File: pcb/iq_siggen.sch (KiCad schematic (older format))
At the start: 109 parts, among them J1 J3 - BANK0, J10 Barrel_Jack_MountingPin, J11 Conn_Coaxial, J12 Conn_01x01_Male, J13 Conn_01x01_Male, J14 Conn_01x01_Male, J15 Conn_01x01_Male, J16 Conn_01x01_Male, J17 Conn_01x01_Male, J2 J4 - BANK1, J3 Conn_01x20_Male, J4 Conn_01x01_Male, J6 Conn_Coaxial, J7 Conn_Coaxial, J8 Conn_Coaxial, J9 Conn_Coaxial, SW1 SW_Push, SW2 SW_Push, SW3 SW_Push, SW4 SW_Push, U1 AMS1117-3.3, U2 TPS72325DBVR, U3 TLV73325PDBVT

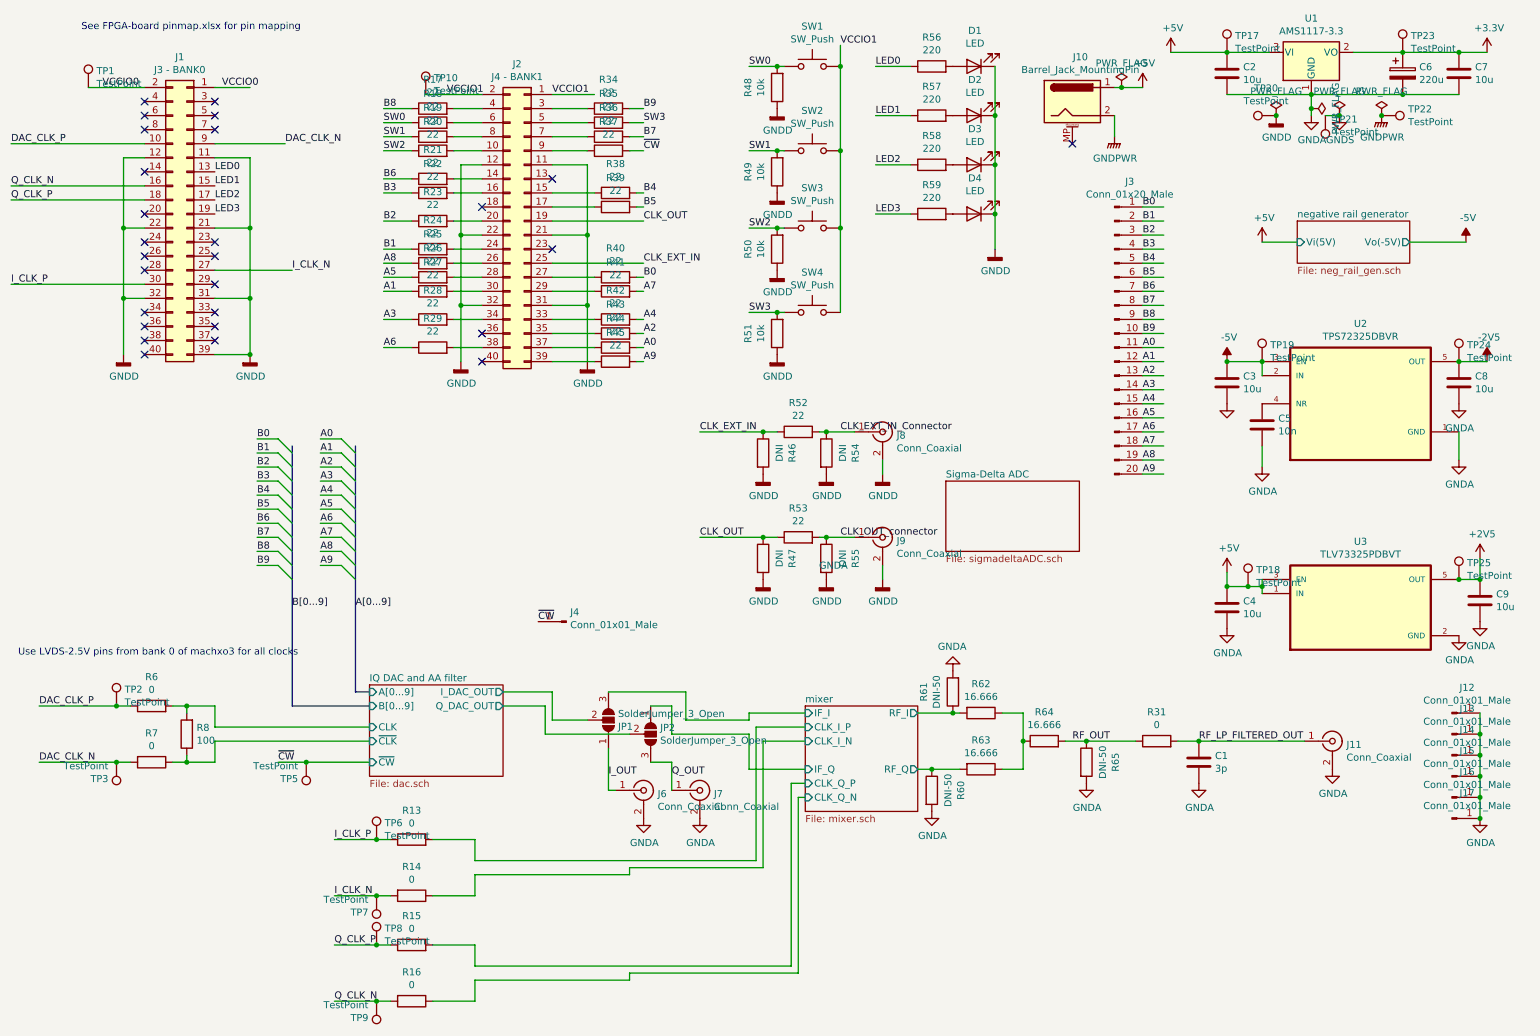
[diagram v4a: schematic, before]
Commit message: routing contiued, add swtiches, remove test points, all parts now positioned on board
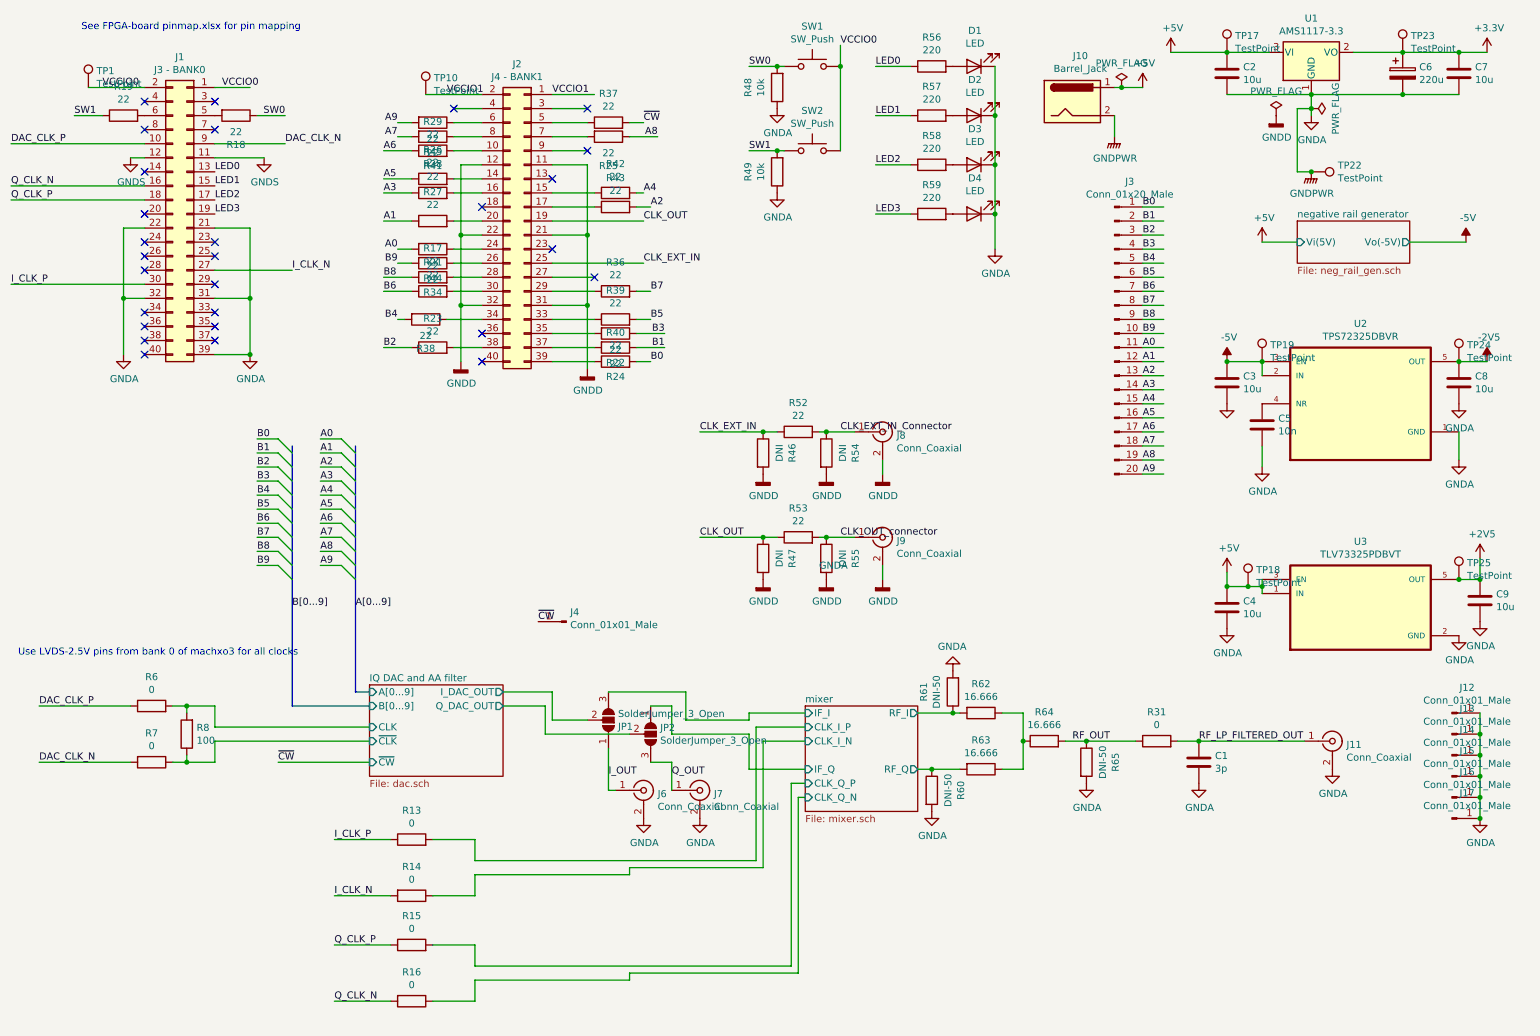
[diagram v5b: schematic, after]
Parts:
- removed J10: Barrel_Jack_MountingPin, Connector_BarrelJack:BarrelJack_Horizontal, symbol Connector:Barrel_Jack_MountingPin
- removed R20, R35: 22, Resistor_SMD:R_0603_1608Metric, symbol Device:R
- removed R50, R51: 10k, Resistor_SMD:R_0603_1608Metric, symbol Device:R
- removed SW3, SW4: SW_Push, symbol Switch:SW_Push
- removed TP2, TP20, TP21, TP3, TP5, TP6, TP7, TP8, TP9: TestPoint, TestPoint:TestPoint_Pad_D1.5mm, symbol Connector:TestPoint
- added J10: Barrel_Jack, Connector_BarrelJack:BarrelJack_Horizontal, symbol Connector:Barrel_Jack
- SW1, SW2: footprint (none) -> Button_Switch_THT:SW_PUSH_6mm_H5mm
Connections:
- net labels removed: SW2, SW3
- wire segments 270 -> 255
- no-connect marks 27 -> 28
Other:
- moved on the sheet: R17, R18, R19, R21, R22, R23, R24, R25, R26, R27, R28, R29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

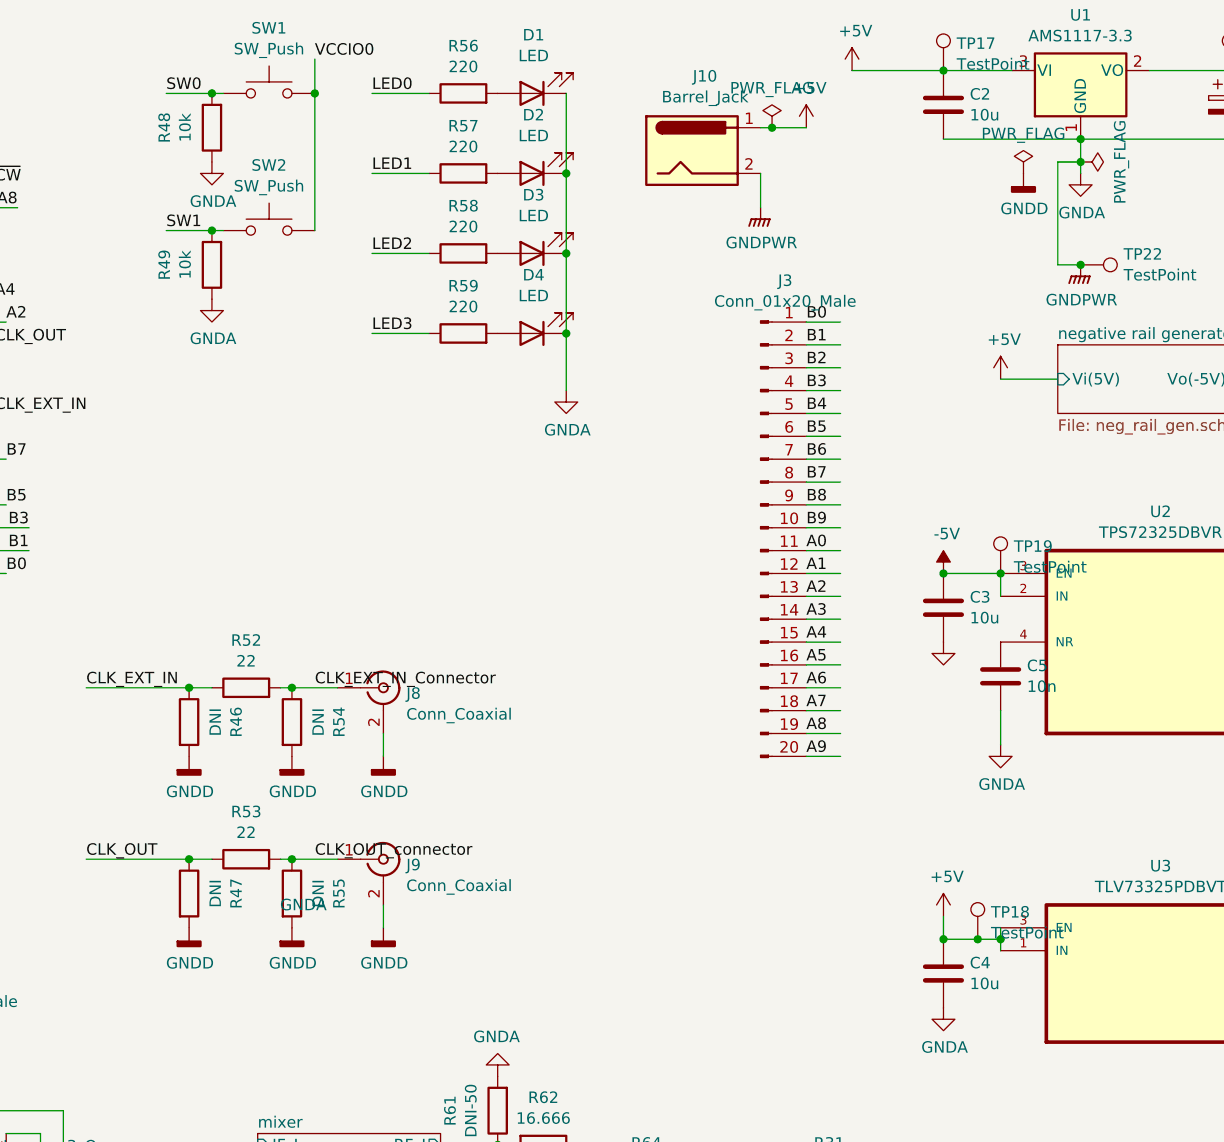
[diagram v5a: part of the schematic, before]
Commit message: layout refininements, stitching vias
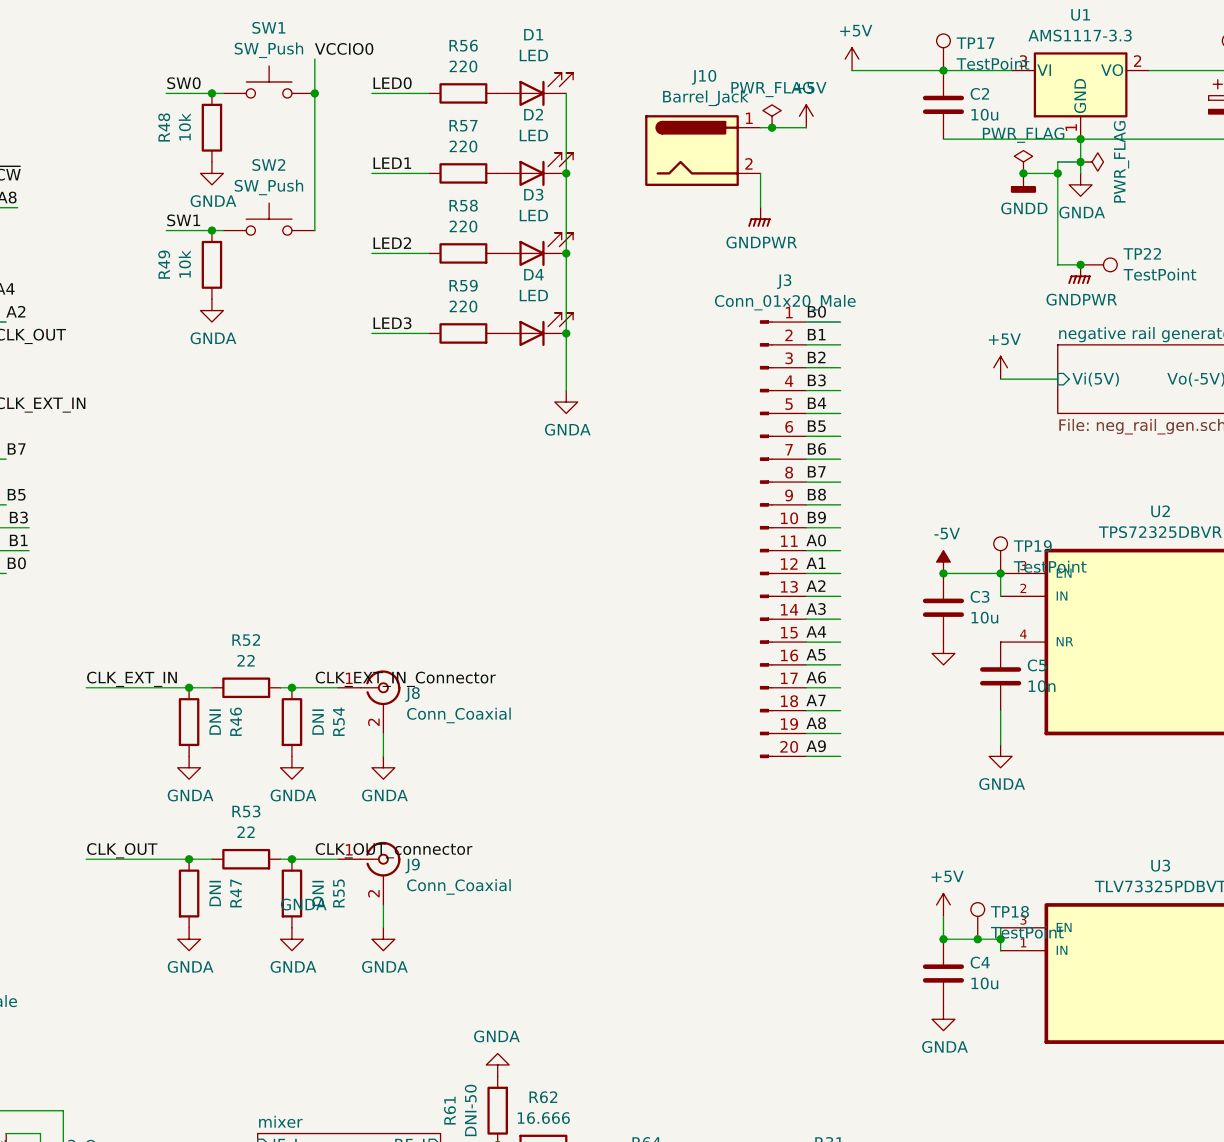
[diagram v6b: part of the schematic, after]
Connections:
- wire segments 255 -> 257
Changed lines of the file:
@@
 Text Label 5400 3550 0    50   ~ 0
 CLK_EXT_IN
-$Comp
-L power:GNDD #PWR017
-U 1 1 608214B8
-P 6700 3850
-AR Path="/608214B8" Ref="#PWR017"  Part="1"
-AR Path="/5FB3742F/608214B8" Ref="#PWR?"  Part="1"
-F 0 "#PWR017" H 6700 3600 50  0001 C CNN
-F 1 "GNDD" H 6704 3695 50  0000 C CNN
-F 2 "" H 6700 3850 50  0001 C CNN
-F 3 "" H 6700 3850 50  0001 C CNN
-	1    6700 3850
-	1    0    0    -1
-$EndComp
 Wire Wire Line
 	6500 3550 6300 3550
@@
 Wire Wire Line
 	5850 3550 5400 3550
-$Comp
-L power:GNDD #PWR015
-U 1 1 60891A86
-P 6300 3850
-AR Path="/60891A86" Ref="#PWR015"  Part="1"
-AR Path="/5FB3742F/60891A86" Ref="#PWR?"  Part="1"
-F 0 "#PWR015" H 6300 3600 50  0001 C CNN
-F 1 "GNDD" H 6304 3695 50  0000 C CNN
-F 2 "" H 6300 3850 50  0001 C CNN
-F 3 "" H 6300 3850 50  0001 C CNN
-	1    6300 3850
-	1    0    0    -1
-$EndComp
-$Comp
-L power:GNDD #PWR09
-U 1 1 60891D84
-P 5850 3850
-AR Path="/60891D84" Ref="#PWR09"  Part="1"
-AR Path="/5FB3742F/60891D84" Ref="#PWR?"  Part="1"
-F 0 "#PWR09" H 5850 3600 50  0001 C CNN
-F 1 "GNDD" H 5854 3695 50  0000 C CNN
-F 2 "" H 5850 3850 50  0001 C CNN
-F 3 "" H 5850 3850 50  0001 C CNN
-	1    5850 3850
-	1    0    0    -1
-$EndComp
 Wire Wire Line
 	6700 3750 6700 3850
@@
 $EndComp
 $Comp
-L power:GNDD #PWR018
-U 1 1 60998D71
-P 6700 4600
-AR Path="/60998D71" Ref="#PWR018"  Part="1"
-AR Path="/5FB3742F/60998D71" Ref="#PWR?"  Part="1"
-F 0 "#PWR018" H 6700 4350 50  0001 C CNN
-F 1 "GNDD" H 6704 4445 50  0000 C CNN
-F 2 "" H 6700 4600 50  0001 C CNN
-F 3 "" H 6700 4600 50  0001 C CNN
-	1    6700 4600
-	1    0    0    -1
-$EndComp
-$Comp
 L Device:R R53
 U 1 1 60998D77
@@
 Wire Wire Line
 	5850 4300 5400 4300
-$Comp
-L power:GNDD #PWR016
-U 1 1 60998D8F
-P 6300 4600
-AR Path="/60998D8F" Ref="#PWR016"  Part="1"
-AR Path="/5FB3742F/60998D8F" Ref="#PWR?"  Part="1"
-F 0 "#PWR016" H 6300 4350 50  0001 C CNN
-F 1 "GNDD" H 6304 4445 50  0000 C CNN
-F 2 "" H 6300 4600 50  0001 C CNN
-F 3 "" H 6300 4600 50  0001 C CNN
-	1    6300 4600
-	1    0    0    -1
-$EndComp
-$Comp
-L power:GNDD #PWR010
-U 1 1 60998D95
-P 5850 4600
-AR Path="/60998D95" Ref="#PWR010"  Part="1"
-AR Path="/5FB3742F/60998D95" Ref="#PWR?"  Part="1"
-F 0 "#PWR010" H 5850 4350 50  0001 C CNN
-F 1 "GNDD" H 5854 4445 50  0000 C CNN
-F 2 "" H 5850 4600 50  0001 C CNN
-F 3 "" H 5850 4600 50  0001 C CNN
-	1    5850 4600
-	1    0    0    -1
-$EndComp
 Wire Wire Line
 	6700 4500 6700 4600
@@
 	9750 1700 9650 1700
 Wire Wire Line
-	9650 1700 9650 1250
+	9650 1700 9650 1300
 Wire Wire Line
 	9650 1250 9750 1250
@@
 Wire Wire Line
 	2400 5900 3050 5900
+$Comp
+L power:GNDA #PWR0116
+U 1 1 5FCC926F
+P 5850 3850
+F 0 "#PWR0116" H 5850 3600 50  0001 C CNN
+F 1 "GNDA" H 5855 3677 50  0000 C CNN
+F 2 "" H 5850 3850 50  0001 C CNN
+F 3 "" H 5850 3850 50  0001 C CNN
+	1    5850 3850
+	1    0    0    -1
+$EndComp
+$Comp
+L power:GNDA #PWR0117
+U 1 1 5FCC9A73
+P 6300 3850
+F 0 "#PWR0117" H 6300 3600 50  0001 C CNN
+F 1 "GNDA" H 6305 3677 50  0000 C CNN
+F 2 "" H 6300 3850 50  0001 C CNN
+F 3 "" H 6300 3850 50  0001 C CNN
+	1    6300 3850
+	1    0    0    -1
+$EndComp
+$Comp
+L power:GNDA #PWR0118
+U 1 1 5FCC9CC6
+P 6700 3850
+F 0 "#PWR0118" H 6700 3600 50  0001 C CNN
+F 1 "GNDA" H 6705 3677 50  0000 C CNN
+F 2 "" H 6700 3850 50  0001 C CNN
+F 3 "" H 6700 3850 50  0001 C CNN
+	1    6700 3850
+	1    0    0    -1
+$EndComp
+$Comp
+L power:GNDA #PWR0119
+U 1 1 5FCC9F56
+P 6700 4600
+F 0 "#PWR0119" H 6700 4350 50  0001 C CNN
+F 1 "GNDA" H 6705 4427 50  0000 C CNN
+F 2 "" H 6700 4600 50  0001 C CNN
+F 3 "" H 6700 4600 50  0001 C CNN
+	1    6700 4600
+	1    0    0    -1
+$EndComp
+$Comp
+L power:GNDA #PWR0120
+U 1 1 5FCCA3FC
+P 6300 4600
+F 0 "#PWR0120" H 6300 4350 50  0001 C CNN
+F 1 "GNDA" H 6305 4427 50  0000 C CNN
+F 2 "" H 6300 4600 50  0001 C CNN
+F 3 "" H 6300 4600 50  0001 C CNN
+	1    6300 4600
+	1    0    0    -1
+$EndComp
+$Comp
+L power:GNDA #PWR0121
+U 1 1 5FCCA6B1
+P 5850 4600
+F 0 "#PWR0121" H 5850 4350 50  0001 C CNN
+F 1 "GNDA" H 5855 4427 50  0000 C CNN
+F 2 "" H 5850 4600 50  0001 C CNN
+F 3 "" H 5850 4600 50  0001 C CNN
+	1    5850 4600
+	1    0    0    -1
+$EndComp
+Wire Wire Line
+	9500 1300 9650 1300
 Wire Bus Line
 	2500 3650 2500 5500
 Wire Bus Line
 	2950 3650 2950 5400
+Connection ~ 9500 1300
+Connection ~ 9650 1300
+Wire Wire Line
+	9650 1300 9650 1250
 $EndSCHEMATC

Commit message: clean up, label sub circuit blocks in silkscreen document the expected clock and baseband amplitudes based on opamp gains
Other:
- note added: "+/- 350mV differential \n1.25V common mode voltage"
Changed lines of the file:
@@
 Wire Wire Line
 	9500 1300 9650 1300
+Connection ~ 9500 1300
+Connection ~ 9650 1300
+Wire Wire Line
+	9650 1300 9650 1250
+Text Notes 1500 6200 0    50   ~ 0
++/- 350mV differential \n1.25V common mode voltage
 Wire Bus Line
 	2500 3650 2500 5500
 Wire Bus Line
 	2950 3650 2950 5400
-Connection ~ 9500 1300
-Connection ~ 9650 1300
-Wire Wire Line
-	9650 1300 9650 1250
 $EndSCHEMATC
